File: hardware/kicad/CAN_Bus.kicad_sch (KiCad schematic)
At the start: 3 parts

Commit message: Phase A3: hierarchical V1 schematic generated from pstxnet.dat, ERC clean, netlist == pstxnet
gen_symbols.py (R1240N001x, TCAN1042H-Q1, CMS06 diode, VIN_RAW power symbol per current datasheets),
kicad_sym.py (flattened embedding of KiCad 9 library symbols), gen_sch.py (7 sub-sheets mirroring the OrCAD
blocks, labels/hierarchical pins/power symbols, deterministic symbol paths shared with the PCB via v1_design.py),
check_netlist.py (schematic and board nets == pstxnet.dat, refs and footprint paths match).
ERC 0 violations with --severity-all. Allegro refdes without a trailing digit get a '1' suffix (KiCad annotation
rule); original kept in the Allegro_RefDes property.

Co-Authored-By: Claude Fable 5.1 <noreply@anthropic.com>
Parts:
- removed _TEMPLATE_C: C_TEMPLATE, symbol Device:C
- removed _TEMPLATE_D: LED_TEMPLATE, symbol Device:LED
- removed _TEMPLATE_R: R_TEMPLATE, symbol Device:R
- added C1: 1uF, LoRa_Boat_Controller:CAP_KGM21_KAV-L, symbol Device:C
- added CANHEADER1: B4B-XH-A, LoRa_Boat_Controller:CONN_B4B-XH-A_JST, symbol Connector_Generic:Conn_01x04
- added U5: TCAN1042HDRQ1, LoRa_Boat_Controller:D0008A_L, symbol LoRa_Boat_Controller:TCAN1042H-Q1
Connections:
- new net CANH: CANHEADER1.4 (Pin_4), U5.6 (CANL)
- new net CANL: CANHEADER1.3 (Pin_3), U5.7 (CANH)
- new net CAN_RXD_PA10: U5.4 (RXD)
- new net CAN_STB_PA11: U5.8 (STB)
- new net CAN_TXD_PA12: U5.1 (TXD)
- new net CAN_VCC: C1.2, CANHEADER1.2 (Pin_2), U5.3 (VCC)
- new net GND: C1.1, CANHEADER1.1 (Pin_1), U5.2 (GND)
- no-connect marks 0 -> 1
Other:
- note added: "Allegro net names: CANH<-N04855, CANL<-N24691, CAN_RXD_PA10<-N04759, CAN_STB_PA11<-N04755, CAN_TXD_PA12<-N04763, CAN_VCC<-N24886, GND<-0"
- note added: "CAN_Bus: OrCAD block: CANBUS module (TCAN1042H-Q1, C1, JST XH header; VCC supplied through the header)"
- note added: "PWR_FLAG: CAN_VCC (TCAN1042H VCC, 4.5-5.5 V) is supplied externally through CANHEADER pin 2"
- company: (none) -> University of Arkansas EECS
- title: (none) -> LoRa Autonomous Boat Controller V1 - CAN_Bus

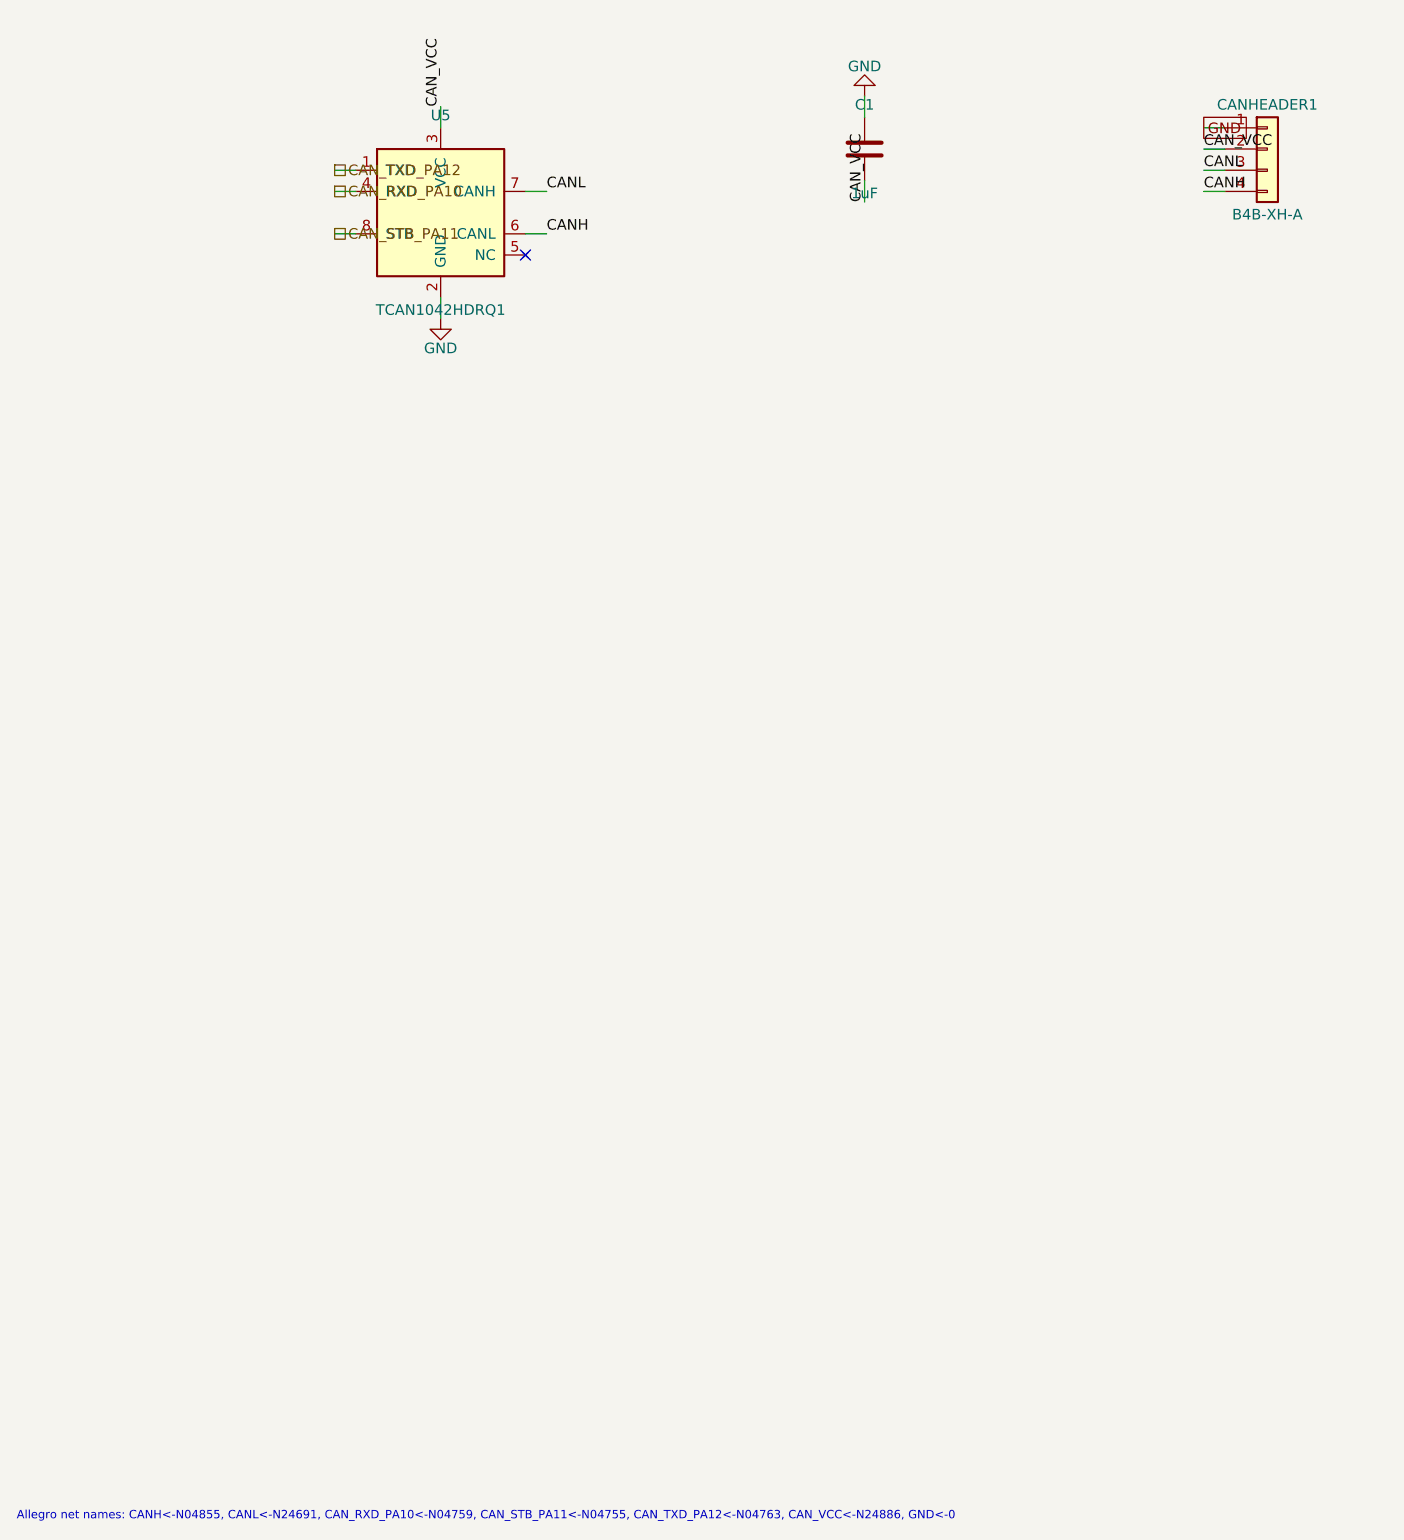
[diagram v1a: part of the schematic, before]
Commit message: Phase A3 close: CANH/CANL net names corrected, BOM with MPNs, DSN-v2 comparison, schematic exports
- gen_pcb.py: N04855 is CANL (U5 pin 6) and N24691 is CANH (U5 pin 7) per pstxnet.dat + TI SLLSES9D; the
  old NETLIST.md had them reversed (Codex review finding R03).
- gen_bom.py: docs/BOM.csv regenerated from the schematic with MPN/manufacturer/description/confidence/price
  columns (research in docs/research/BOM_MPN_RESEARCH.md, prices 2026-09-16).
- a0_xor_dsn.py: DSN v2 copper vs v5 films = 54 % / 63 % mismatch, 0 of 20 vias coincide, 0 of 45 parts unmoved;
  the DSN wiring is unusable for v5 (documented in docs/A0_PROVENANCE.md).
- Schematic PDF and per-sheet SVG exports in docs/img.
Gates: DRC 0 errors / 0 unconnected, ERC 0 violations, netlist check PASS, XOR F.Cu 0.87 % B.Cu 0.23 %.

Co-Authored-By: Claude Fable 5.1 <noreply@anthropic.com>
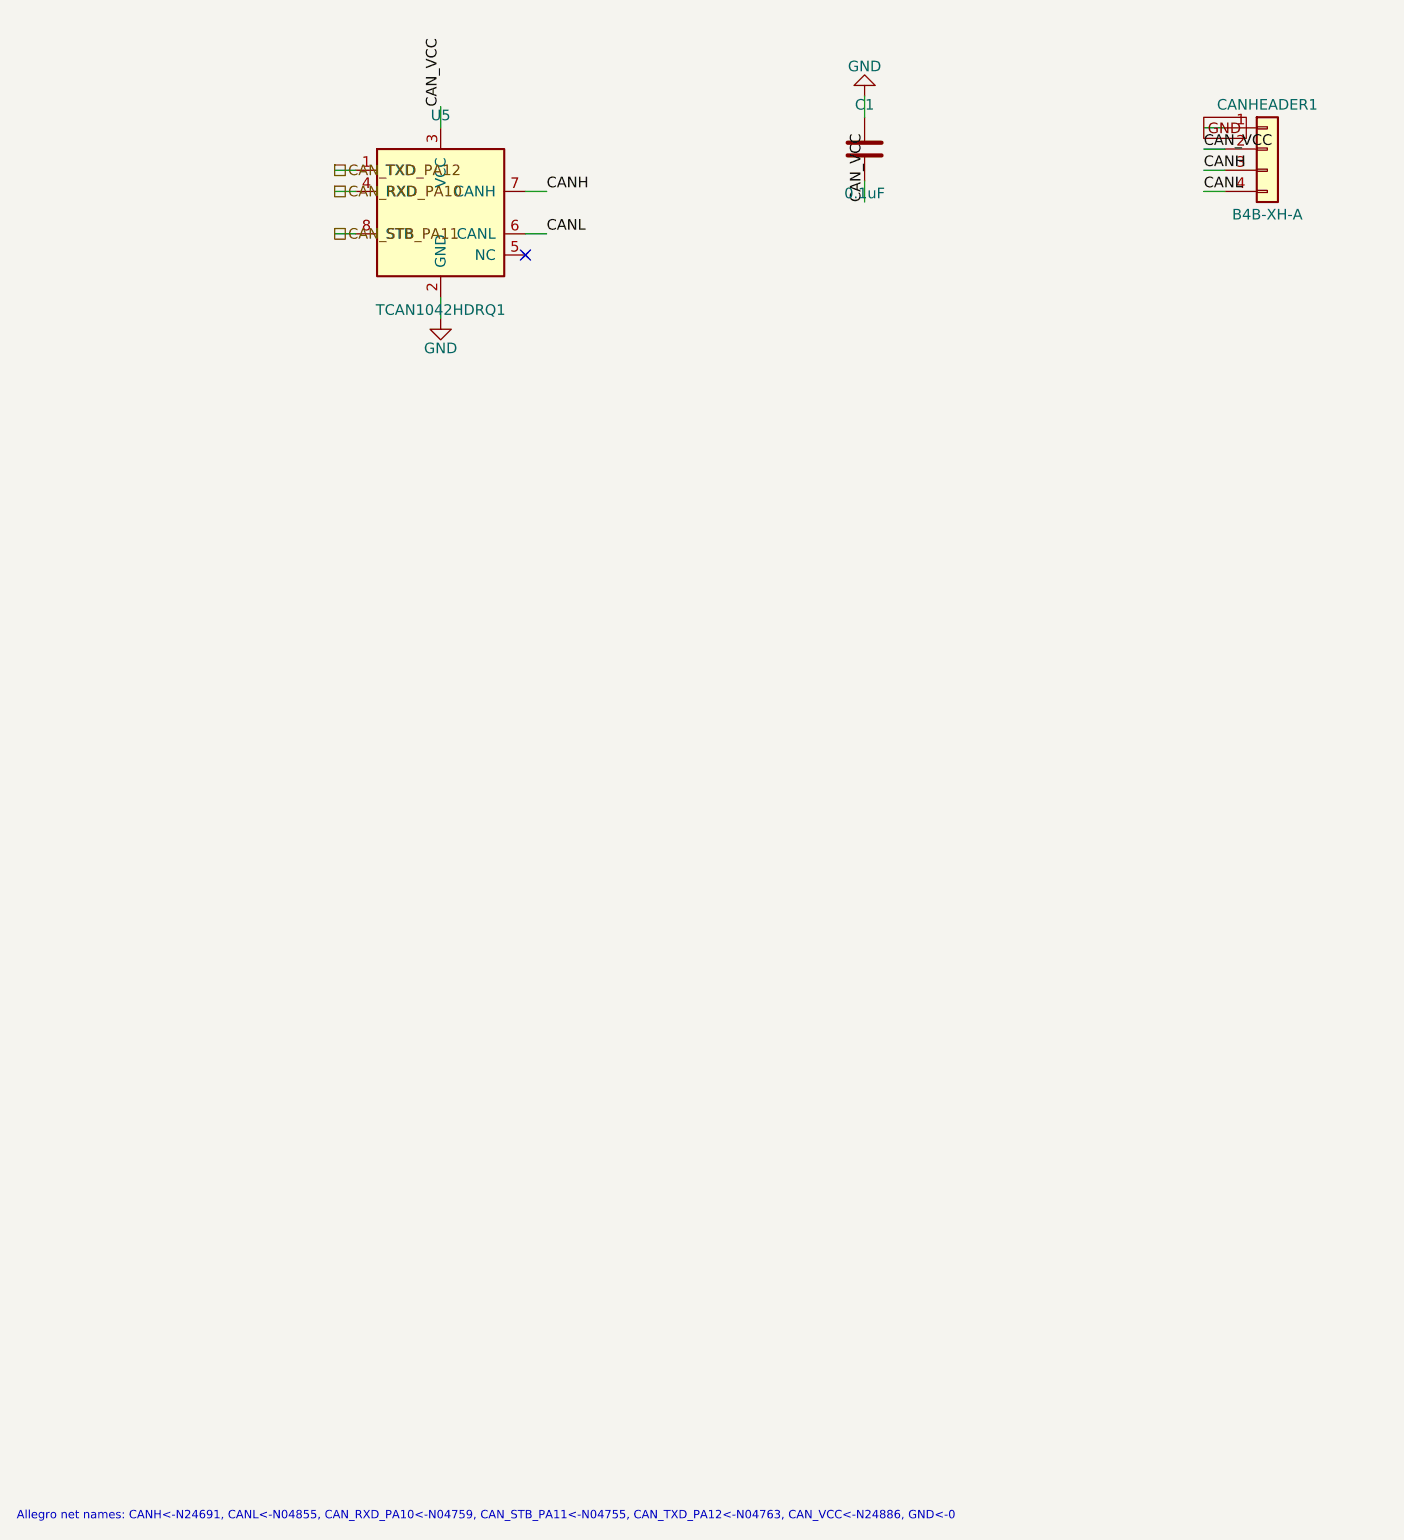
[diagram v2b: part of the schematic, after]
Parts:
- C1: value 1uF -> 0.1uF; MPN (none) -> KGM21NR71H104KT; Manufacturer (none) -> Kyocera AVX
- CANHEADER1: MPN (none) -> B4B-XH-A(LF)(SN); Manufacturer (none) -> JST
- U5: MPN (none) -> TCAN1042HDRQ1; Manufacturer (none) -> Texas Instruments
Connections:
- net CANH: now also CANHEADER1.3 (Pin_3), U5.7 (CANH); no longer CANHEADER1.4 (Pin_4), U5.6 (CANL)
- net CANL: now also CANHEADER1.4 (Pin_4), U5.6 (CANL); no longer CANHEADER1.3 (Pin_3), U5.7 (CANH)
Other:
- note added: "Allegro net names: CANH<-N24691, CANL<-N04855, CAN_RXD_PA10<-N04759, CAN_STB_PA11<-N04755, CAN_TXD_PA12<-N04763, CAN_VCC<-N24886, GND<-0"
- note removed: "Allegro net names: CANH<-N04855, CANL<-N24691, CAN_RXD_PA10<-N04759, CAN_STB_PA11<-N04755, CAN_TXD_PA12<-N04763, CAN_VCC<-N24886, GND<-0"
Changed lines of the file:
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@@
 			)
 		)
-		(property "Description" "Automotive CAN FD transceiver, 5 V VCC (4.5-5.5 V), SOIC-8. Pins per TI SLLSES9D. STB has internal pull-up (HIGH = standby)."
+		(property "Description" "Automotive CAN FD transceiver, 5 V VCC, SOIC-8 (Mouser flags EOL; TI successor TCAN1044A-Q1)"
 			(at 63.5 43.18 0)
 			(effects
@@
 		)
 		(property "Allegro_Device" "TCAN1042HDRQ1_D0008A_L_TCAN1042H-Q1D"
+			(at 63.5 43.18 0)
+			(effects
+				(font
+					(size 1.27 1.27)
+				)
+				(hide yes)
+			)
+		)
+		(property "MPN" "TCAN1042HDRQ1"
+			(at 63.5 43.18 0)
+			(effects
+				(font
+					(size 1.27 1.27)
+				)
+				(hide yes)
+			)
+		)
+		(property "Manufacturer" "Texas Instruments"
 			(at 63.5 43.18 0)
 			(effects
@@
 		)
 	)
+	(label "CANH"
+		(at 76.2 40.64 0)
+		(effects
+			(font
+				(size 1.27 1.27)
+			)
+			(justify left bottom)
+		)
+	)
+	(wire
+		(pts
+			(xy 73.66 45.72) (xy 76.2 45.72)
+		)
+		(stroke
+			(width 0)
+			(type default)
+		)
+	)
 	(label "CANL"
-		(at 76.2 40.64 0)
-		(effects
-			(font
-				(size 1.27 1.27)
-			)
-			(justify left bottom)
-		)
-	)
-	(wire
-		(pts
-			(xy 73.66 45.72) (xy 76.2 45.72)
-		)
-		(stroke
-			(width 0)
-			(type default)
-		)
-	)
-	(label "CANH"
 		(at 76.2 45.72 0)
 		(effects
@@
 			)
 		)
-		(property "Value" "1uF"
+		(property "Value" "0.1uF"
 			(at 114.3 40.87 0)
 			(effects
@@
 			)
 		)
-		(property "Description" "Unpolarized capacitor"
+		(property "Description" "0.1 uF 10% 50 V X7R MLCC 0805"
 			(at 114.3 35.56 0)
 			(effects
@@
 		)
 		(property "Allegro_Device" "C_CAP_KGM21_KAV-L_.1UF"
+			(at 114.3 35.56 0)
+			(effects
+				(font
+					(size 1.27 1.27)
+				)
+				(hide yes)
+			)
+		)
+		(property "MPN" "KGM21NR71H104KT"
+			(at 114.3 35.56 0)
+			(effects
+				(font
+					(size 1.27 1.27)
+				)
+				(hide yes)
+			)
+		)
+		(property "Manufacturer" "Kyocera AVX"
 			(at 114.3 35.56 0)
 			(effects
@@
 			)
 		)
-		(property "Description" "Generic connector, single row, 01x04, script generated (kicad-library-utils/schlib/autogen/connector/)"
+		(property "Description" "XH 2.5 mm 4-position vertical through-hole header"
 			(at 162.56 35.56 0)
 			(effects
@@
 		)
 		(property "Allegro_Device" "B4B-XH-A_CONN_B4B-XH-A_JST_CONN_B4B-XH-A"
+			(at 162.56 35.56 0)
+			(effects
+				(font
+					(size 1.27 1.27)
+				)
+				(hide yes)
+			)
+		)
+		(property "MPN" "B4B-XH-A(LF)(SN)"
+			(at 162.56 35.56 0)
+			(effects
+				(font
+					(size 1.27 1.27)
+				)
+				(hide yes)
+			)
+		)
+		(property "Manufacturer" "JST"
 			(at 162.56 35.56 0)
 			(effects
@@
 		)
 	)
+	(label "CANH"
+		(at 154.94 38.1 180)
+		(effects
+			(font
+				(size 1.27 1.27)
+			)
+			(justify left bottom)
+		)
+	)
+	(wire
+		(pts
+			(xy 157.48 40.64) (xy 154.94 40.64)
+		)
+		(stroke
+			(width 0)
+			(type default)
+		)
+	)
 	(label "CANL"
-		(at 154.94 38.1 180)
-		(effects
-			(font
-				(size 1.27 1.27)
-			)
-			(justify left bottom)
-		)
-	)
-	(wire
-		(pts
-			(xy 157.48 40.64) (xy 154.94 40.64)
-		)
-		(stroke
-			(width 0)
-			(type default)
-		)
-	)
-	(label "CANH"
 		(at 154.94 40.64 180)
 		(effects
@@
 		)
 	)
-	(text "Allegro net names: CANH<-N04855, CANL<-N24691, CAN_RXD_PA10<-N04759, CAN_STB_PA11<-N04755, CAN_TXD_PA12<-N04763, CAN_VCC<-N24886, GND<-0"
+	(text "Allegro net names: CANH<-N24691, CANL<-N04855, CAN_RXD_PA10<-N04759, CAN_STB_PA11<-N04755, CAN_TXD_PA12<-N04763, CAN_VCC<-N24886, GND<-0"
 		(exclude_from_sim no)
 		(at 12.7 200 0)
